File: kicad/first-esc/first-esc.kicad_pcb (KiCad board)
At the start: 2 copper layers, 117 parts, among them J1 Conn_ARM_JTAG_SWD_10, J2 USB_OTG, J3 Supply, J4 Gnd, J5 PH_A, J6 PH_B, J7 PH_C, Q1 Q_NMOS_GDS, Q2 Q_NMOS_GDS, Q3 Q_NMOS_GDS, Q4 Q_NMOS_GDS, Q5 Q_NMOS_GDS, Q6 Q_NMOS_GDS, U1 DRV8302DCAR, U2 INA240A2PW, U3 INA240A2PW, U4 INA240A2PW, U5 BL1551, U6 BL1551, U7 BL1551, U8 AMS1117-3.3, U9 STM32F405RGTx, Y1 8M

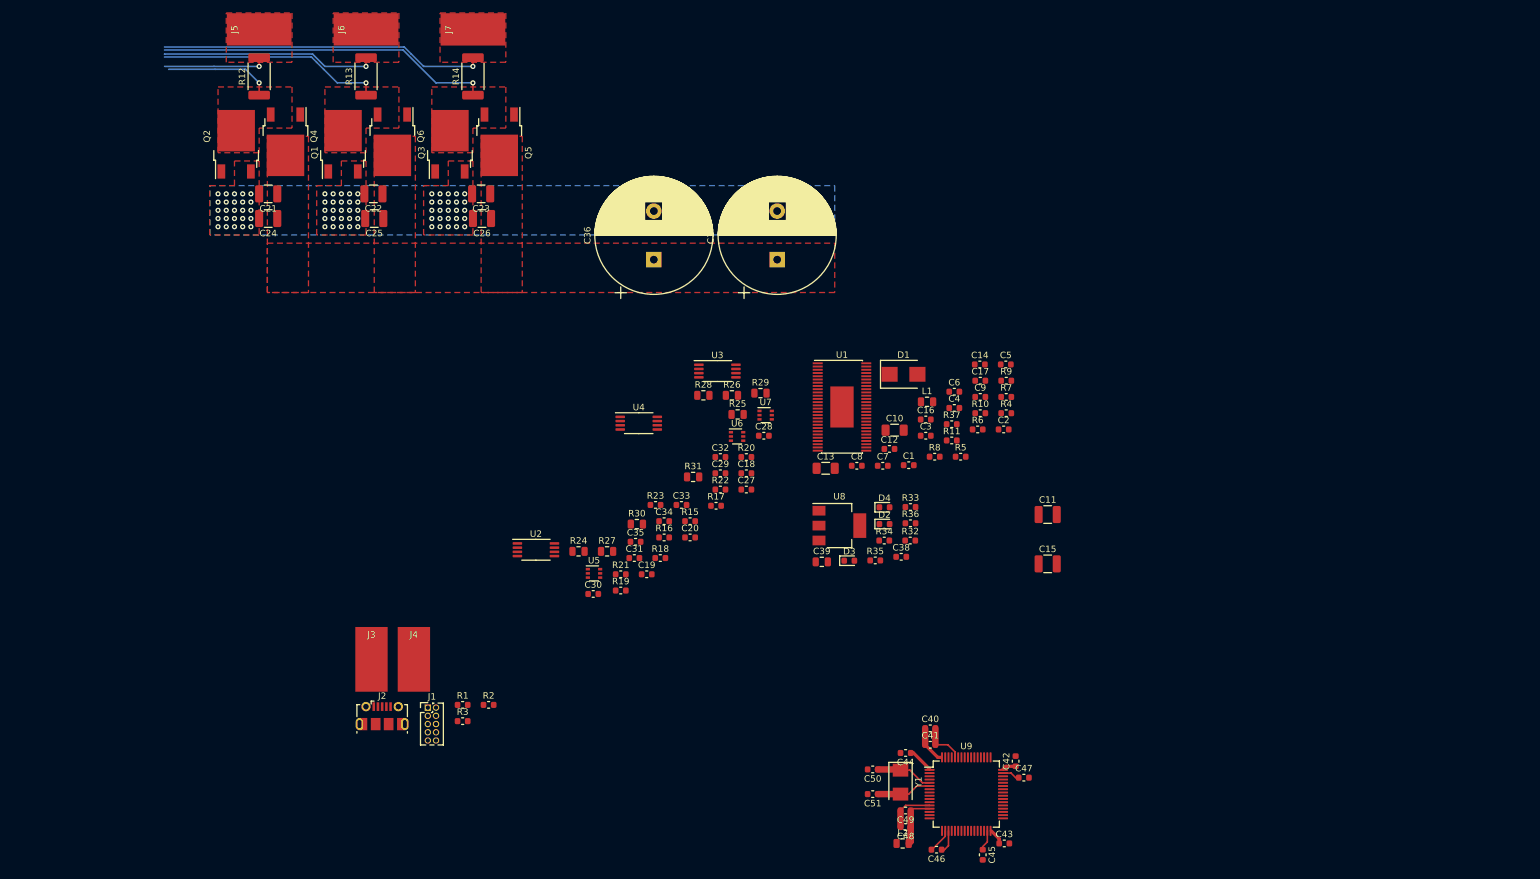
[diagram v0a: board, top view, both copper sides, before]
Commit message: mostly finished up DRV and MCU pcb layout
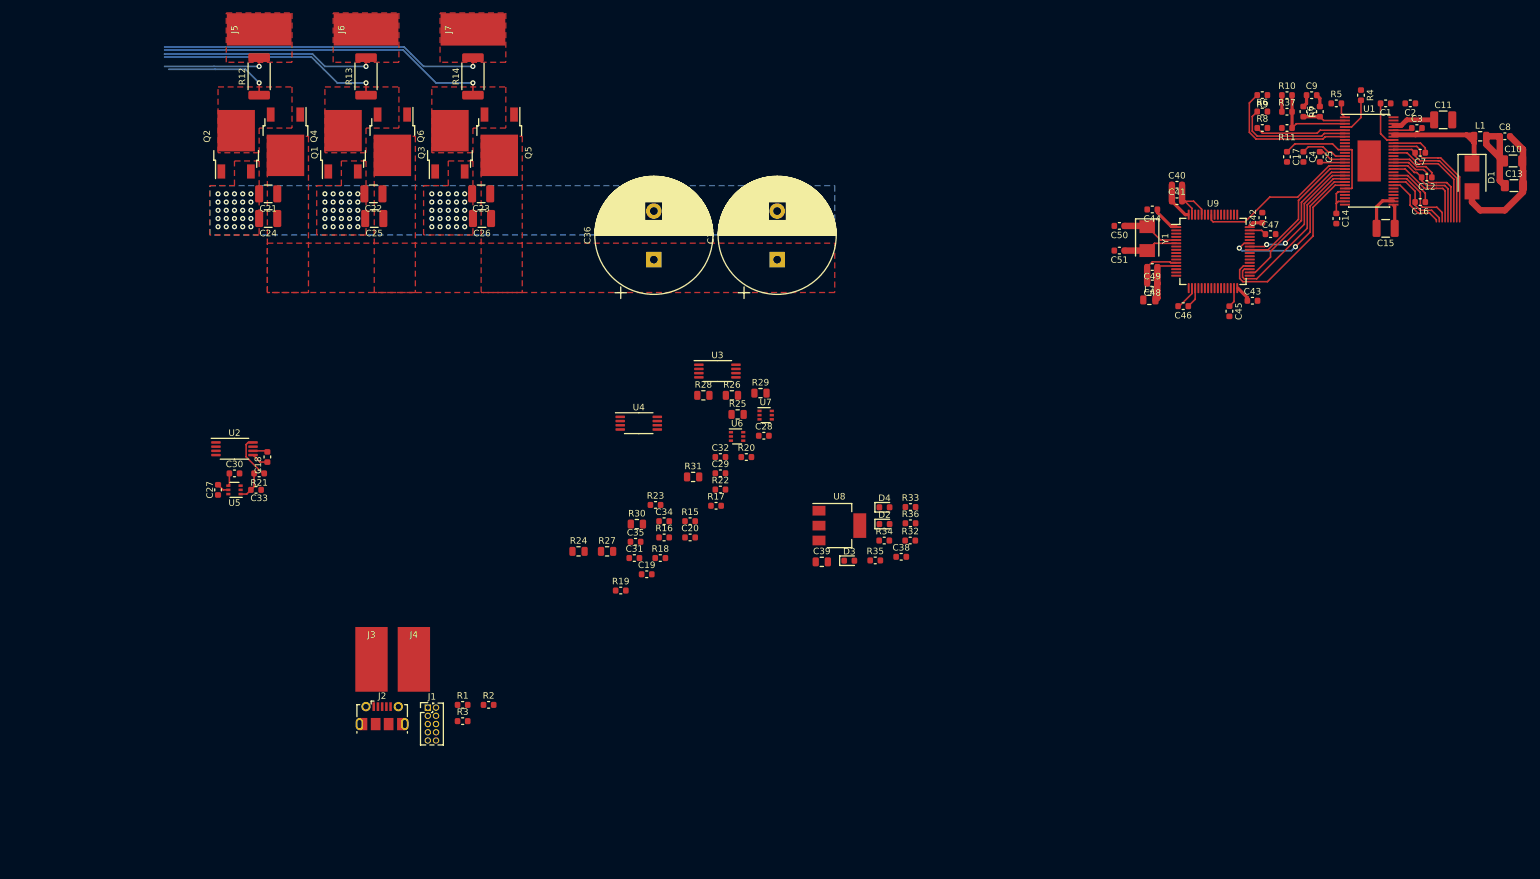
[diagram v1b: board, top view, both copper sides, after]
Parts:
- moved C13 114.9 mm to (270.0, 48.3)
- moved C8 112.3 mm to (268.6, 40.6)
- moved C10 104.2 mm to (269.9, 44.5)
- moved C7 96.1 mm to (255.5, 43.2), turned to 180 degrees
- moved L1 94.8 mm to (264.8, 40.6)
- moved C12 93.0 mm to (256.5, 47.0), turned to 180 degrees
- moved D1 92.9 mm to (263.5, 47.0), turned to 270 degrees
- moved C1 92.5 mm to (250.2, 35.6), turned to 180 degrees
- moved C40 92.2 mm to (218.0, 48.1)
- moved C41 92.2 mm to (218.0, 50.7)
- moved C42 92.2 mm to (231.1, 53.2)
- moved C45 92.2 mm to (226.1, 67.7)
- moved C48 92.2 mm to (214.1, 63.4)
- moved C49 92.2 mm to (214.1, 60.8)
- moved C50 92.2 mm to (209.1, 54.5)
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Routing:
- net GND: track 18.1 -> 54.6 mm
- net /GateDriver/INL_C: track 0.00 -> 28.4 mm
- net /GateDriver/INL_B: track 0.00 -> 26.6 mm
- net +3V3: track 18.0 -> 43.5 mm
- net /GateDriver/EN_GATE: track 0.00 -> 25.2 mm
- net /MCU/H_C: track 0.00 -> 25.1 mm, vias 0 -> 2
- net /GateDriver/INL_A: track 0.00 -> 23.3 mm
- net /MCU/H_A: track 0.00 -> 21.6 mm
- net /GateDriver/DTC: track 0.00 -> 21.6 mm
- net /MCU/H_B: track 0.00 -> 21.1 mm, vias 0 -> 2
- net /GateDriver/PH: track 0.00 -> 20.1 mm
- net /GateDriver/GH_A: track 0.00 -> 19.6 mm
- net /GateDriver/SH_A: track 16.7 -> 35.4 mm
- net Net-(R6-Pad1): track 0.00 -> 18.1 mm
- net /GateDriver/DVDD: track 0.00 -> 17.9 mm
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
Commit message: checkpoint before redoing mcu and drv
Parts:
- C36, C37, J4: moved to B.Cu
- moved C1 160.3 mm to (103.5, 100.3)
- moved C10 160.3 mm to (123.2, 109.2)
- moved C11 160.3 mm to (112.4, 102.9)
- moved C12 160.3 mm to (109.9, 111.8)
- moved C13 160.3 mm to (123.3, 113.0)
- moved C14 160.3 mm to (95.9, 118.1)
- moved C15 160.3 mm to (103.5, 119.6)
- moved C16 160.3 mm to (108.8, 115.6)
- moved C17 160.3 mm to (88.3, 108.6)
- moved C2 160.3 mm to (107.3, 100.3)
- moved C3 160.3 mm to (108.3, 104.1)
- moved C4 160.3 mm to (90.8, 108.6)
- moved C40 160.3 mm to (71.3, 112.9)
- moved C41 160.3 mm to (71.3, 115.4)
- moved C42 160.3 mm to (84.5, 118.0)
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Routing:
- net +3V3: track 43.5 -> 52.7 mm
- net /Power/CURR_C_RAW: track 0.00 -> 6.96 mm
- net /Power/CURR_B_RAW: track 0.00 -> 6.96 mm
- net /CURR_C: track 0.00 -> 4.60 mm
- net /CURR_B: track 0.00 -> 4.60 mm
- net GND: track 54.6 -> 59.2 mm
- net Net-(C31-Pad1): track 0.00 -> 1.96 mm
- net Net-(C32-Pad1): track 0.00 -> 1.96 mm
- net /Power/PH_A: vias 1 -> 37
- net /GateDriver/SH_A: vias 1 -> 28
- added copper zone on B.Cu, net /GateDriver/SH_A
- added copper zone on B.Cu, net /Power/PH_A
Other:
- rule trace_min: 0.2 -> 0.127
- rule via_min_drill: 0.3 -> 0.2
- rule via_min_size: 0.4 -> 0.45

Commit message: removed traces
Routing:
- net /GateDriver/INL_C: track 28.4 -> 0.00 mm
- net /GateDriver/INL_B: track 26.6 -> 0.00 mm
- net /GateDriver/EN_GATE: track 25.2 -> 0.00 mm
- net /MCU/H_C: track 25.1 -> 0.00 mm, vias 2 -> 0
- net /GateDriver/INL_A: track 23.3 -> 0.00 mm
- net /MCU/H_A: track 21.6 -> 0.00 mm
- net /MCU/H_B: track 21.1 -> 0.00 mm, vias 2 -> 0
- net /GateDriver/GH_A: track 19.6 -> 0.00 mm
- net /GateDriver/SH_A: track 35.4 -> 16.7 mm
- net /GateDriver/GL_A: track 17.6 -> 0.00 mm
- net /GateDriver/GH_B: track 16.5 -> 0.00 mm
- net /GateDriver/SH_B: track 49.9 -> 34.7 mm
- net /GateDriver/GL_B: track 14.2 -> 0.00 mm
- net /GateDriver/GH_C: track 12.3 -> 0.00 mm
- net /GateDriver/SH_C: track 62.9 -> 51.6 mm
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
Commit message: kinda coming together?
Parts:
- moved C13 106.2 mm to (49.5, 36.7), turned to 90 degrees
- moved C10 106.0 mm to (45.7, 36.8), turned to 90 degrees
- moved C8 104.6 mm to (41.9, 38.1), turned to 90 degrees
- moved L1 99.2 mm to (41.9, 41.9), turned to 90 degrees
- moved D1 97.0 mm to (48.3, 43.2), turned to 0 degrees
- moved C11 87.5 mm to (42.5, 50.2), turned to 180 degrees
- moved C16 86.0 mm to (55.2, 48.3), turned to 270 degrees
- moved C12 85.4 mm to (52.7, 48.3), turned to 270 degrees
- moved C7 83.7 mm to (50.2, 48.3), turned to 270 degrees
- moved C3 82.4 mm to (46.4, 49.8), turned to 90 degrees
- moved C2 80.8 mm to (40.6, 54.6), turned to 90 degrees
- moved C15 77.2 mm to (61.8, 54.6), turned to 270 degrees
- moved C1 76.2 mm to (42.5, 54.6), turned to 270 degrees
- moved J2 75.1 mm to (73.0, 88.3)
- moved R2 75.1 mm to (89.4, 86.5)
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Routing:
- net /GateDriver/SH_B: track 34.7 -> 115.8 mm, vias 1 -> 32
- net /Power/CURR_FILTER: track 0.00 -> 81.1 mm, vias 0 -> 4
- net /GateDriver/SH_C: track 51.6 -> 121.9 mm, vias 1 -> 32
- net /CURR_C: track 4.60 -> 71.6 mm, vias 0 -> 2
- net Net-(Q5-Pad1): track 0.00 -> 65.3 mm, vias 0 -> 2
- net /GateDriver/SH_A: track 16.7 -> 79.7 mm, vias 28 -> 30
- net /CURR_B: track 4.60 -> 63.6 mm, vias 0 -> 2
- net /CURR_A: track 4.60 -> 63.4 mm, vias 0 -> 4
- net Net-(Q6-Pad1): track 0.00 -> 48.0 mm, vias 0 -> 2
- net Net-(Q3-Pad1): track 0.00 -> 47.8 mm, vias 0 -> 2
- net Net-(Q1-Pad1): track 0.00 -> 29.8 mm, vias 0 -> 2
- net Net-(Q4-Pad1): track 0.00 -> 29.7 mm, vias 0 -> 2
- net /VOLT_C: track 0.00 -> 27.2 mm, vias 0 -> 2
- net /VOLT_B: track 0.00 -> 25.1 mm, vias 0 -> 2
- net /VOLT_A: track 0.00 -> 23.2 mm, vias 0 -> 2
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- added copper zone on B.Cu, net /GateDriver/SH_B
- added copper zone on B.Cu, net /GateDriver/SH_C
- added copper zone on B.Cu, net /Power/PH_B
- added copper zone on B.Cu, net /Power/PH_C
